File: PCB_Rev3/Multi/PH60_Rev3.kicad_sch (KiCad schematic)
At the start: 47 parts, among them J1 Conn_01x02_Pin, J2 Conn_01x02_Pin, J3 USB_C_Receptacle_USB2.0_16P, J4 Conn_01x04_Socket, U1 TP4057, U2 nRF52840, U4 TPS2116DRL, X1 32.768kHz, X2 Crystal_Generic

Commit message: 上传遗漏
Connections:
- net col_1: now also U2.A10 (AIN5/P0.29); no longer U2.P23 (P1.07)
- net col_2: now also U2.A12 (AIN0/P0.02); no longer U2.T23 (P1.05)
- net row_0: now also U2.A16 (P1.13); no longer U2.Y23 (P1.01)
- net row_1: now also U2.A20 (P1.10); no longer U2.AD22 (TRACEDATA0/P1.00)

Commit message: Wires update
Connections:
- no-connect marks 21 -> 29
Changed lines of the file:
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@@
+	)
+	(no_connect
+		(at 284.48 144.78)
 	)
 	(no_connect
@@
 	(no_connect
 		(at 284.48 124.46)
+	)
+	(no_connect
+		(at 284.48 111.76)
 	)
 	(no_connect
@@
 	)
 	(no_connect
+		(at 284.48 127)
+	)
+	(no_connect
 		(at 233.68 43.18)
 	)
@@
 	(no_connect
 		(at 284.48 152.4)
+	)
+	(no_connect
+		(at 284.48 139.7)
+	)
+	(no_connect
+		(at 284.48 132.08)
+	)
+	(no_connect
+		(at 284.48 58.42)
 	)
 	(no_connect
@@
 	)
 	(no_connect
+		(at 284.48 134.62)
+	)
+	(no_connect
 		(at 52.07 67.31)
 	)
+	(no_connect
+		(at 284.48 149.86)
+	)
 	(wire

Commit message: DRC checked
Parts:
- C23: footprint (none) -> Capacitor_SMD:C_0402_1005Metric
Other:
- note added: "Daughterboard connector (DNP)"
- note removed: "Daughterboard connector"
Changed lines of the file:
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@@
 		)
 	)
-	(text "Daughterboard connector"
+	(text "Daughterboard connector\n(DNP)"
 		(exclude_from_sim no)
 		(at 39.37 143.51 0)
@@
 		(exclude_from_sim no)
 		(in_bom yes)
-		(on_board yes)
+		(on_board no)
 		(dnp no)
 		(fields_autoplaced yes)
@@
 		(exclude_from_sim no)
 		(in_bom yes)
-		(on_board yes)
+		(on_board no)
 		(dnp no)
 		(fields_autoplaced yes)
@@
 		(exclude_from_sim no)
 		(in_bom yes)
-		(on_board yes)
+		(on_board no)
 		(dnp no)
 		(fields_autoplaced yes)
@@
 			)
 		)
-		(property "Footprint" ""
+		(property "Footprint" "Capacitor_SMD:C_0402_1005Metric"
 			(at 88.5952 265.43 0)
 			(effects

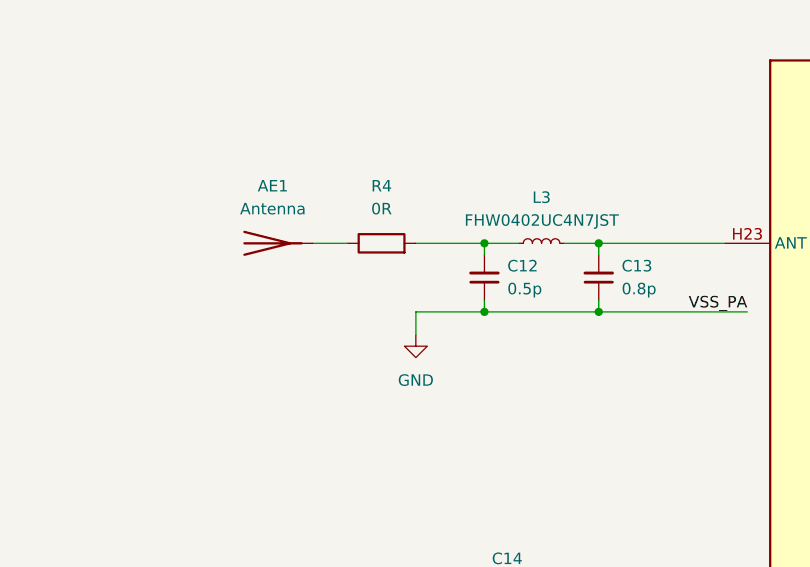
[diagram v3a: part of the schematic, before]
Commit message: Redesign antenna and space switch
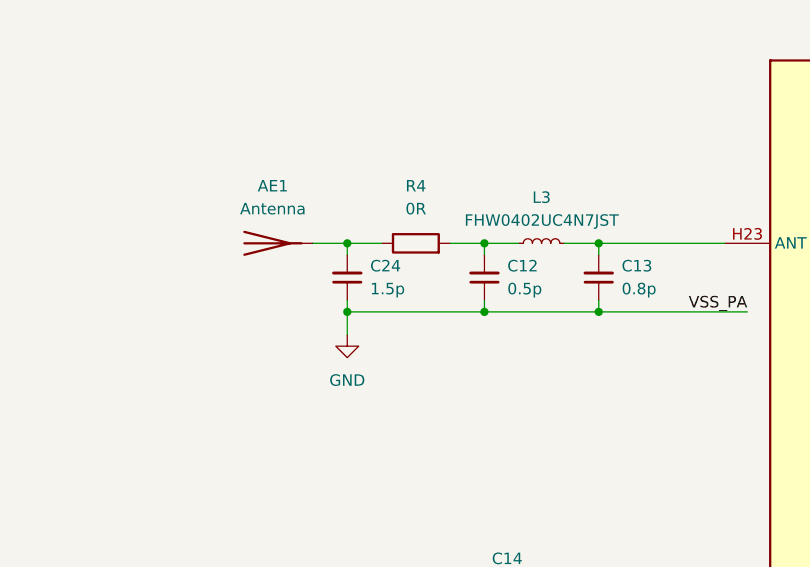
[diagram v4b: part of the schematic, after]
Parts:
- added C24: 1.5p, Capacitor_SMD:C_0402_1005Metric, symbol Device:C_Small
- R4: footprint PCM_Resistor_SMD_AKL:R_0603_1608Metric -> Capacitor_SMD:C_0402_1005Metric
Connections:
- net GND: now also C24.1
- net at AE1.1 (A), R4.1: now also C24.2
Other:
- moved on the sheet: R4
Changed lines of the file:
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@@
 	)
 	(junction
+		(at 176.53 76.2)
+		(diameter 0)
+		(color 0 0 0 0)
+	)
+	(junction
 		(at 227.33 214.63)
 		(diameter 0)
@@
 	)
 	(junction
+		(at 176.53 68.58)
+		(diameter 0)
+		(color 0 0 0 0)
+	)
+	(junction
 		(at 196.85 113.03)
 		(diameter 0)
@@
 	(wire
 		(pts
-			(xy 184.15 68.58) (xy 191.77 68.58)
+			(xy 187.96 68.58) (xy 191.77 68.58)
 		)
 		(stroke
@@
 	(wire
 		(pts
-			(xy 184.15 76.2) (xy 191.77 76.2)
-		)
-		(stroke
-			(width 0)
-			(type default)
-		)
-	)
-	(wire
-		(pts
 			(xy 200.66 120.65) (xy 209.55 120.65)
 		)
@@
 	(wire
 		(pts
-			(xy 184.15 76.2) (xy 184.15 78.74)
+			(xy 176.53 76.2) (xy 176.53 78.74)
 		)
 		(stroke
@@
 	(wire
 		(pts
+			(xy 176.53 68.58) (xy 180.34 68.58)
+		)
+		(stroke
+			(width 0)
+			(type default)
+		)
+	)
+	(wire
+		(pts
 			(xy 218.44 120.65) (xy 218.44 119.38)
 		)
@@
 	(wire
 		(pts
+			(xy 176.53 76.2) (xy 191.77 76.2)
+		)
+		(stroke
+			(width 0)
+			(type default)
+		)
+	)
+	(wire
+		(pts
 			(xy 191.77 109.22) (xy 186.69 109.22)
 		)
@@
 	(wire
 		(pts
+			(xy 176.53 69.85) (xy 176.53 68.58)
+		)
+		(stroke
+			(width 0)
+			(type default)
+		)
+	)
+	(wire
+		(pts
 			(xy 299.72 53.34) (xy 303.53 53.34)
 		)
@@
 	(wire
 		(pts
+			(xy 176.53 74.93) (xy 176.53 76.2)
+		)
+		(stroke
+			(width 0)
+			(type default)
+		)
+	)
+	(wire
+		(pts
 			(xy 106.68 119.38) (xy 116.84 119.38)
 		)
@@
 	(symbol
 		(lib_id "Device:R")
-		(at 180.34 68.58 90)
+		(at 184.15 68.58 90)
 		(unit 1)
 		(exclude_from_sim no)
@@
 		(fields_autoplaced yes)
 		(property "Reference" "R4"
-			(at 180.34 62.23 90)
+			(at 184.15 62.23 90)
 			(effects
 				(font
@@
 		)
 		(property "Value" "0R"
-			(at 180.34 64.77 90)
+			(at 184.15 64.77 90)
 			(effects
 				(font
@@
 			)
 		)
-		(property "Footprint" "PCM_Resistor_SMD_AKL:R_0603_1608Metric"
-			(at 180.34 70.358 90)
+		(property "Footprint" "Capacitor_SMD:C_0402_1005Metric"
+			(at 184.15 70.358 90)
 			(effects
 				(font
@@
 		)
 		(property "Datasheet" "~"
-			(at 180.34 68.58 0)
+			(at 184.15 68.58 0)
 			(effects
 				(font
@@
 		)
 		(property "Description" "Resistor"
-			(at 180.34 68.58 0)
+			(at 184.15 68.58 0)
 			(effects
 				(font
@@
 	)
 	(symbol
+		(lib_id "Device:C_Small")
+		(at 176.53 72.39 180)
+		(unit 1)
+		(exclude_from_sim no)
+		(in_bom yes)
+		(on_board yes)
+		(dnp no)
+		(fields_autoplaced yes)
+		(property "Reference" "C24"
+			(at 179.07 71.1135 0)
+			(effects
+				(font
+					(size 1.27 1.27)
+				)
+				(justify right)
+			)
+		)
+		(property "Value" "1.5p"
+			(at 179.07 73.6535 0)
+			(effects
+				(font
+					(size 1.27 1.27)
+				)
+				(justify right)
+			)
+		)
+		(property "Footprint" "Capacitor_SMD:C_0402_1005Metric"
+			(at 176.53 72.39 0)
+			(effects
+				(font
+					(size 1.27 1.27)
+				)
+				(hide yes)
+			)
+		)
+		(property "Datasheet" "~"
+			(at 176.53 72.39 0)
+			(effects
+				(font
+					(size 1.27 1.27)
+				)
+				(hide yes)
+			)
+		)
+		(property "Description" "Unpolarized capacitor, small symbol"
+			(at 176.53 72.39 0)
+			(effects
+				(font
+					(size 1.27 1.27)
+				)
+				(hide yes)
+			)
+		)
+		(pin "2"
+		)
+		(pin "1"
+		)
+		(instances
+			(project "PH60_Rev3"
+				(path "/dca0f898-8fdb-4522-a51d-f4f4238906e7"
+					(reference "C24")
+					(unit 1)
+				)
+			)
+		)
+	)
+	(symbol
 		(lib_id "Device:R")
 		(at 41.91 177.8 0)
@@
 	(symbol
 		(lib_id "power:GND")
-		(at 184.15 78.74 0)
+		(at 176.53 78.74 0)
 		(unit 1)
 		(exclude_from_sim no)
@@
 		(fields_autoplaced yes)
 		(property "Reference" "#PWR011"
-			(at 184.15 85.09 0)
+			(at 176.53 85.09 0)
 			(effects
 				(font
@@
 		)
 		(property "Value" "GND"
-			(at 184.15 83.82 0)
+			(at 176.53 83.82 0)
 			(effects
 				(font
@@
 		)
 		(property "Footprint" ""
-			(at 184.15 78.74 0)
+			(at 176.53 78.74 0)
 			(effects
 				(font
@@
 		)
 		(property "Datasheet" ""
-			(at 184.15 78.74 0)
+			(at 176.53 78.74 0)
 			(effects
 				(font
@@
 		)
 		(property "Description" "Power symbol creates a global label with name \"GND\" , ground"
-			(at 184.15 78.74 0)
+			(at 176.53 78.74 0)
 			(effects
 				(font

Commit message: multi v3 电感调整
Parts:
- removed L4: LQG15HS15NJ02D, Inductor_SMD:L_0402_1005Metric, symbol Device:L_Small
- removed L5: MCL1608S100MT, Inductor_SMD:L_0603_1608Metric, symbol Device:L_Small
- added L2: MCL1608S100MT, Inductor_SMD:L_0603_1608Metric, symbol Device:L_Small
- added L6: LQG15HS15NJ02D, Inductor_SMD:L_0402_1005Metric, symbol Device:L_Small
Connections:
- net DCC: now also L2.1
- net DEC4: now also L6.2
- new net: L2.2, L6.1
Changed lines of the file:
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@@
 	)
 	(junction
-		(at 167.64 209.55)
-		(diameter 0)
-		(color 0 0 0 0)
-	)
-	(junction
 		(at 99.06 254)
 		(diameter 0)
@@
 	)
 	(junction
+		(at 163.83 209.55)
+		(diameter 0)
+		(color 0 0 0 0)
+	)
+	(junction
 		(at 243.84 222.25)
 		(diameter 0)
@@
 	(wire
 		(pts
-			(xy 39.37 250.19) (xy 39.37 254)
+			(xy 163.83 195.58) (xy 157.48 195.58)
 		)
 		(stroke
@@
 	(wire
 		(pts
-			(xy 243.84 214.63) (xy 243.84 215.9)
+			(xy 39.37 250.19) (xy 39.37 254)
 		)
 		(stroke
@@
 	(wire
 		(pts
-			(xy 167.64 195.58) (xy 157.48 195.58)
+			(xy 243.84 214.63) (xy 243.84 215.9)
 		)
 		(stroke
@@
 	(wire
 		(pts
+			(xy 163.83 195.58) (xy 163.83 199.39)
+		)
+		(stroke
+			(width 0)
+			(type default)
+		)
+	)
+	(wire
+		(pts
 			(xy 209.55 157.48) (xy 218.44 157.48)
 		)
@@
 	(wire
 		(pts
-			(xy 167.64 198.12) (xy 167.64 195.58)
-		)
-		(stroke
-			(width 0)
-			(type default)
-		)
-	)
-	(wire
-		(pts
 			(xy 200.66 120.65) (xy 209.55 120.65)
 		)
@@
 	(wire
 		(pts
-			(xy 167.64 209.55) (xy 172.72 209.55)
+			(xy 163.83 209.55) (xy 172.72 209.55)
 		)
 		(stroke
@@
 	(wire
 		(pts
-			(xy 162.56 209.55) (xy 167.64 209.55)
+			(xy 162.56 209.55) (xy 163.83 209.55)
 		)
 		(stroke
@@
 	(wire
 		(pts
-			(xy 167.64 208.28) (xy 167.64 209.55)
-		)
-		(stroke
-			(width 0)
-			(type default)
-		)
-	)
-	(wire
-		(pts
 			(xy 73.66 254) (xy 73.66 259.08)
 		)
@@
 	)
 	(symbol
-		(lib_id "Device:L_Small")
-		(at 167.64 200.66 0)
-		(unit 1)
-		(exclude_from_sim no)
-		(in_bom yes)
-		(on_board yes)
-		(dnp no)
-		(fields_autoplaced yes)
-		(property "Reference" "L4"
-			(at 168.91 199.3899 0)
-			(effects
-				(font
-					(size 1.27 1.27)
-				)
-				(justify left)
-			)
-		)
-		(property "Value" "LQG15HS15NJ02D"
-			(at 168.91 201.9299 0)
-			(effects
-				(font
-					(size 1.27 1.27)
-				)
-				(justify left)
-			)
-		)
-		(property "Footprint" "Inductor_SMD:L_0402_1005Metric"
-			(at 167.64 200.66 0)
-			(effects
-				(font
-					(size 1.27 1.27)
-				)
-				(hide yes)
-			)
-		)
-		(property "Datasheet" "~"
-			(at 167.64 200.66 0)
-			(effects
-				(font
-					(size 1.27 1.27)
-				)
-				(hide yes)
-			)
-		)
-		(property "Description" "Inductor, small symbol"
-			(at 167.64 200.66 0)
-			(effects
-				(font
-					(size 1.27 1.27)
-				)
-				(hide yes)
-			)
-		)
-		(pin "2"
-		)
-		(pin "1"
-		)
-		(instances
-			(project "PH60_Rev3"
-				(path "/dca0f898-8fdb-4522-a51d-f4f4238906e7"
-					(reference "L4")
-					(unit 1)
-				)
-			)
-		)
-	)
-	(symbol
 		(lib_id "Device:R")
 		(at 78.74 265.43 0)
@@
 	)
 	(symbol
+		(lib_id "Device:L_Small")
+		(at 163.83 207.01 0)
+		(unit 1)
+		(exclude_from_sim no)
+		(in_bom yes)
+		(on_board yes)
+		(dnp no)
+		(fields_autoplaced yes)
+		(property "Reference" "L6"
+			(at 165.1 205.7399 0)
+			(effects
+				(font
+					(size 1.27 1.27)
+				)
+				(justify left)
+			)
+		)
+		(property "Value" "LQG15HS15NJ02D"
+			(at 165.1 208.2799 0)
+			(effects
+				(font
+					(size 1.27 1.27)
+				)
+				(justify left)
+			)
+		)
+		(property "Footprint" "Inductor_SMD:L_0402_1005Metric"
+			(at 163.83 207.01 0)
+			(effects
+				(font
+					(size 1.27 1.27)
+				)
+				(hide yes)
+			)
+		)
+		(property "Datasheet" "~"
+			(at 163.83 207.01 0)
+			(effects
+				(font
+					(size 1.27 1.27)
+				)
+				(hide yes)
+			)
+		)
+		(property "Description" "Inductor, small symbol"
+			(at 163.83 207.01 0)
+			(effects
+				(font
+					(size 1.27 1.27)
+				)
+				(hide yes)
+			)
+		)
+		(pin "2"
+		)
+		(pin "1"
+		)
+		(instances
+			(project "PH60_Rev3"
+				(path "/dca0f898-8fdb-4522-a51d-f4f4238906e7"
+					(reference "L6")
+					(unit 1)
+				)
+			)
+		)
+	)
+	(symbol
 		(lib_id "Device:R")
 		(at 184.15 68.58 90)
@@
 	)
 	(symbol
+		(lib_id "Device:L_Small")
+		(at 163.83 201.93 0)
+		(unit 1)
+		(exclude_from_sim no)
+		(in_bom yes)
+		(on_board yes)
+		(dnp no)
+		(fields_autoplaced yes)
+		(property "Reference" "L2"
+			(at 165.1 200.6599 0)
+			(effects
+				(font
+					(size 1.27 1.27)
+				)
+				(justify left)
+			)
+		)
+		(property "Value" "MCL1608S100MT"
+			(at 165.1 203.1999 0)
+			(effects
+				(font
+					(size 1.27 1.27)
+				)
+				(justify left)
+			)
+		)
+		(property "Footprint" "Inductor_SMD:L_0603_1608Metric"
+			(at 163.83 201.93 0)
+			(effects
+				(font
+					(size 1.27 1.27)
+				)
+				(hide yes)
+			)
+		)
+		(property "Datasheet" "~"
+			(at 163.83 201.93 0)
+			(effects
+				(font
+					(size 1.27 1.27)
+				)
+				(hide yes)
+			)
+		)
+		(property "Description" "Inductor, small symbol"
+			(at 163.83 201.93 0)
+			(effects
+				(font
+					(size 1.27 1.27)
+				)
+				(hide yes)
+			)
+		)
+		(pin "2"
+		)
+		(pin "1"
+		)
+		(instances
+			(project "PH60_Rev3"
+				(path "/dca0f898-8fdb-4522-a51d-f4f4238906e7"
+					(reference "L2")
+					(unit 1)
+				)
+			)
+		)
+	)
+	(symbol
 		(lib_id "Device:C_Small")
 		(at 246.38 27.94 0)
@@
 					(unit 1)
 				)
-			)
-		)
-	)
-	(symbol
-		(lib_id "Device:L_Small")
-		(at 167.64 205.74 0)
-		(unit 1)
-		(exclude_from_sim no)
-		(in_bom yes)
-		(on_board yes)
-		(dnp no)
-		(fields_autoplaced yes)
-		(property "Reference" "L5"
-			(at 168.91 204.4699 0)
-			(effects
-				(font
-					(size 1.27 1.27)
-				)
-				(justify left)
-			)
-		)
-		(property "Value" "MCL1608S100MT"
-			(at 168.91 207.0099 0)
-			(effects
-				(font
-					(size 1.27 1.27)
-				)
-				(justify left)
-			)
-		)
-		(property "Footprint" "Inductor_SMD:L_0603_1608Metric"
-			(at 167.64 205.74 0)
-			(effects
-				(font
-					(size 1.27 1.27)
-				)
-				(hide yes)
-			)
-		)
-		(property "Datasheet" "~"
-			(at 167.64 205.74 0)
-			(effects
-				(font
-					(size 1.27 1.27)
-				)
-				(hide yes)
-			)
-		)
-		(property "Description" "Inductor, small symbol"
-			(at 167.64 205.74 0)
-			(effects
-				(font
-					(size 1.27 1.27)
-				)
-				(hide yes)
-			)
-		)
-		(pin "2"
-		)
-		(pin "1"
-		)
-		(instances
-			(project "PH60_Rev3"
-				(path "/dca0f898-8fdb-4522-a51d-f4f4238906e7"
-					(reference "L5")
-					(unit 1)
-				)
